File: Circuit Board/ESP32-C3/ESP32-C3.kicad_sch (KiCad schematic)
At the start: 44 parts

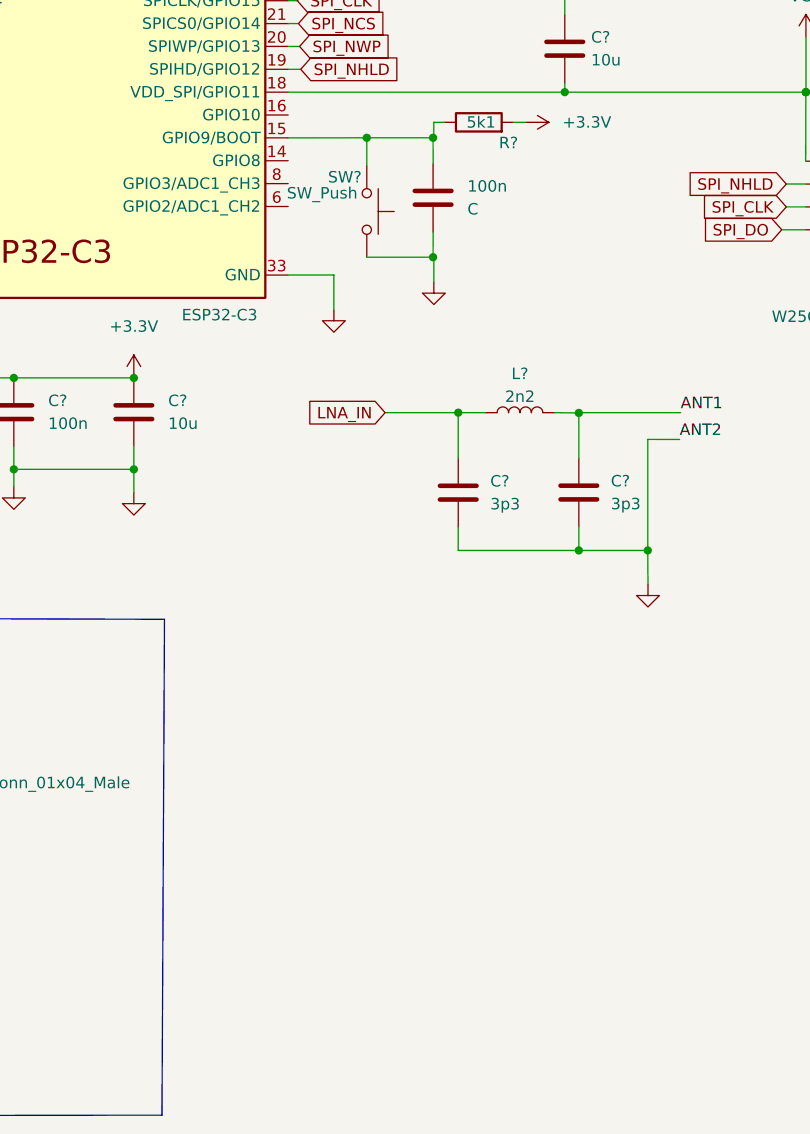
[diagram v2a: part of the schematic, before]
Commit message: Added LED circuits
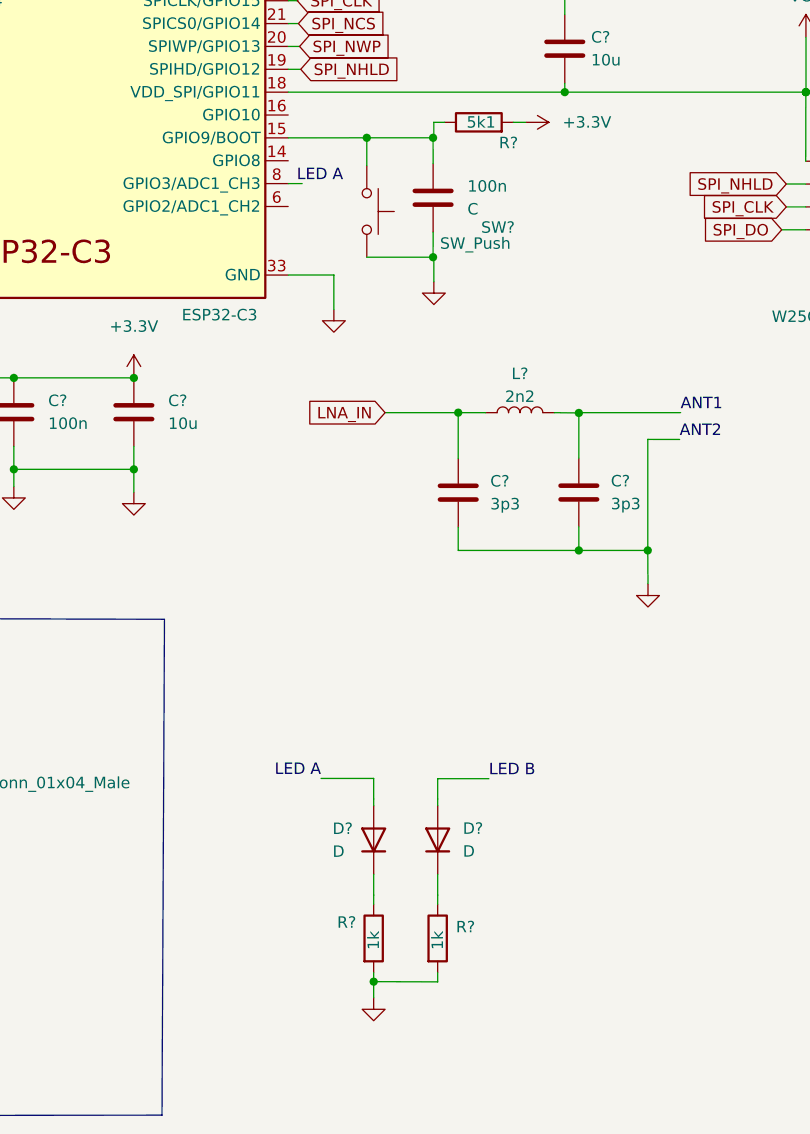
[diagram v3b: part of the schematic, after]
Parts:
- added D? (x2): D, symbol Device:D
- added R? (x2): 1k, symbol Device:R
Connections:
- net +3.3V: now also R?.2, R?.2
- net LED B: now also D?.2 (A)
- net LED A: now reaches U?.8 (GPIO3/ADC1_CH3)
- net LED A: now also D?.2 (A)
- new net: D?.1 (K), R?.1 (x2)

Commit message: Added comments
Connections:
- net at U?.4 (I/O2): now also J?.A6 (D+), J?.B6 (D+)
- no-connect marks 5 -> 8
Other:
- note added: "External 4MB Flash"
- company: (none) -> Sebastian Rincon
- title: (none) -> ESP32-C3
- moved on the sheet: C?, D?, L?, R?

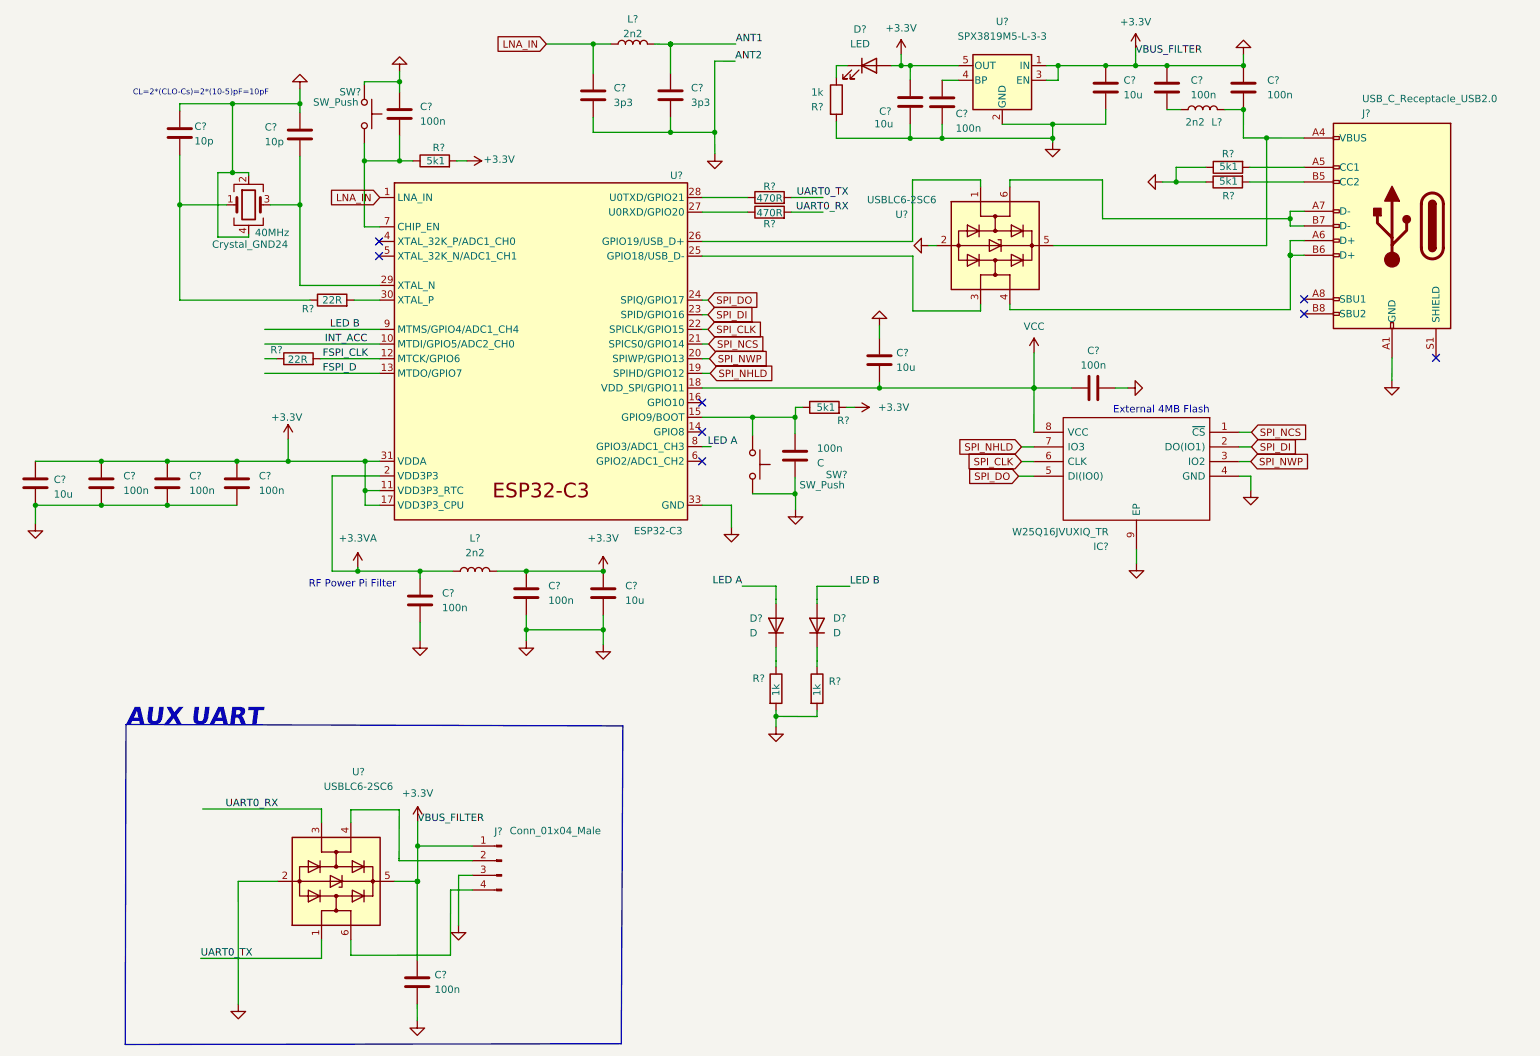
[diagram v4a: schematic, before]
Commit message: Annotated designators
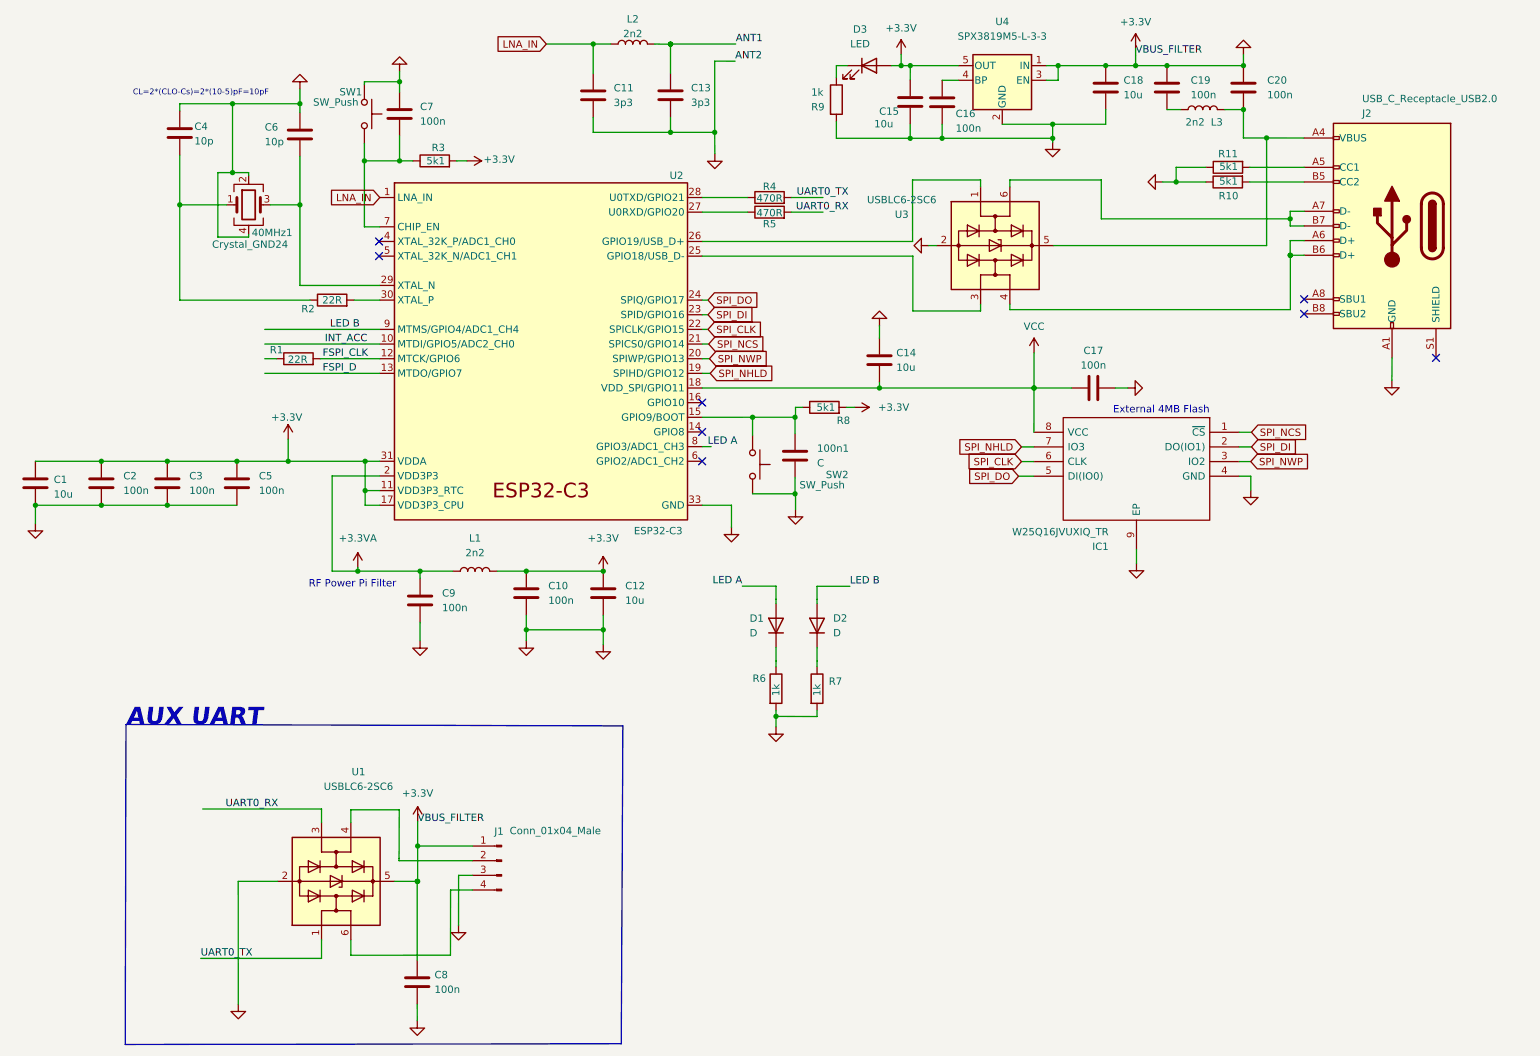
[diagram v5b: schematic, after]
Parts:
- gave numbers to parts that had none: 46
- renumbered 100n to 100n1, 40MHz to 40MHz1

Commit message: Correct ERC errors
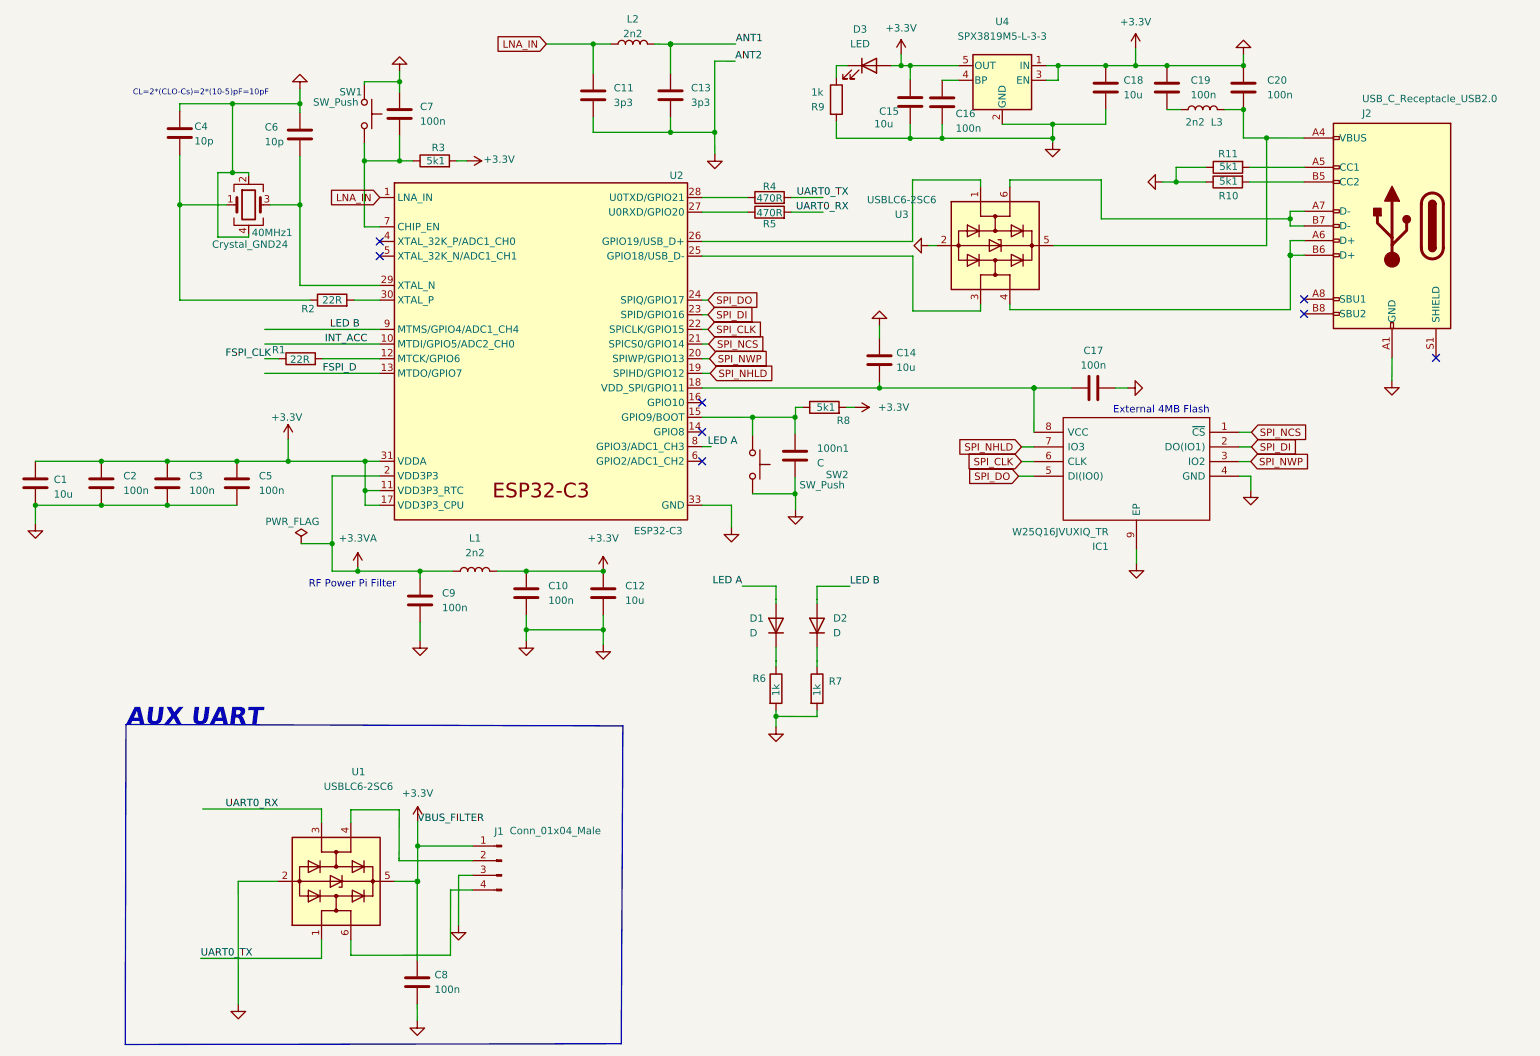
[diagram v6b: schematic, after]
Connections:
- net FSPI_CLK: now also R1.1; no longer R1.2, U2.12 (MTCK/GPIO6)
- net VCC: no longer names the net of C14.2, C17.1, IC1.8 (VCC), U2.18 (VDD_SPI/GPIO11)
- new net: R1.2, U2.12 (MTCK/GPIO6)
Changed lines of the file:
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@@
   (junction (at 32.1564 99.0092) (diameter 0) (color 0 0 0 0)
   )
+  (junction (at 72.1614 105.664) (diameter 0) (color 0 0 0 0)
+  )
   (junction (at 234.1372 35.3411) (diameter 0) (color 0 0 0 0)
   )
@@
   (junction (at 105.8164 110.4392) (diameter 0) (color 0 0 0 0)
   )
+  (no_connect (at 80.4164 55.8292))
+  (no_connect (at 80.4164 53.2892))
   (no_connect (at 240.6396 63.2968))
   (no_connect (at 240.6396 65.8368))
@@
   (no_connect (at 136.2964 86.3092))
   (no_connect (at 136.2964 91.3892))
-  (no_connect (at 80.2894 55.8292))
-  (no_connect (at 80.2894 53.2892))
   (wire (pts (xy 226.8728 30.4292) (xy 230.124 30.4292))
     (stroke (width 0) (type default) (color 0 0 0 0))
@@
     (stroke (width 0) (type default) (color 0 0 0 0))
   )
+  (wire (pts (xy 70.5104 73.6092) (xy 80.4164 73.6092))
+    (stroke (width 0) (type default) (color 0 0 0 0))
+  )
   (wire (pts (xy 152.4789 82.042) (xy 153.67 82.042))
     (stroke (width 0) (type default) (color 0 0 0 0))
@@
     (stroke (width 0) (type default) (color 0 0 0 0))
   )
-  (wire (pts (xy 193.8274 72.5932) (xy 193.8274 78.6892))
-    (stroke (width 0) (type default) (color 0 0 0 0))
-  )
   (wire (pts (xy 60.4774 68.5292) (xy 80.4164 68.5292))
     (stroke (width 0) (type default) (color 0 0 0 0))
@@
     (stroke (width 0) (type default) (color 0 0 0 0))
   )
+  (wire (pts (xy 72.1614 105.664) (xy 72.1614 110.4392))
+    (stroke (width 0) (type default) (color 0 0 0 0))
+  )
   (wire (pts (xy 172.3623 35.4076) (xy 177.8846 35.4076))
     (stroke (width 0) (type default) (color 0 0 0 0))
@@
     (stroke (width 0) (type default) (color 0 0 0 0))
   )
-  (wire (pts (xy 72.1614 93.9292) (xy 72.1614 110.4392))
+  (wire (pts (xy 72.1614 93.9292) (xy 72.1614 105.664))
     (stroke (width 0) (type default) (color 0 0 0 0))
   )
@@
     (stroke (width 0) (type default) (color 0 0 0 0))
   )
-  (wire (pts (xy 70.1294 73.6092) (xy 80.4164 73.6092))
-    (stroke (width 0) (type default) (color 0 0 0 0))
-  )
   (wire (pts (xy 184.5564 42.6212) (xy 172.7596 42.6212))
     (stroke (width 0) (type default) (color 0 0 0 0))
@@
     (stroke (width 0) (type default) (color 0 0 0 0))
   )
+  (wire (pts (xy 66.802 105.664) (xy 72.1614 105.664))
+    (stroke (width 0) (type default) (color 0 0 0 0))
+  )
   (wire (pts (xy 72.1614 110.4392) (xy 76.6064 110.4392))
     (stroke (width 0) (type default) (color 0 0 0 0))
@@
     (stroke (width 0) (type default) (color 0 0 0 0))
   )
-  (wire (pts (xy 60.4774 73.6092) (xy 62.5094 73.6092))
+  (wire (pts (xy 60.4774 73.6092) (xy 62.8904 73.6092))
     (stroke (width 0) (type default) (color 0 0 0 0))
   )
@@
     (effects (font (size 1.27 1.27)) (justify right bottom))
   )
-  (label "VBUS_FILTER" (at 211.4294 21.0525 0)
-    (effects (font (size 1.27 1.27)) (justify left bottom))
-  )
   (label "VBUS_FILTER" (at 86.9797 154.2376 0)
     (effects (font (size 1.27 1.27)) (justify left bottom))
@@
     (effects (font (size 1.27 1.27)) (justify left bottom))
   )
-  (label "FSPI_CLK" (at 70.5104 73.6092 0)
-    (effects (font (size 1.27 1.27)) (justify left bottom))
+  (label "FSPI_CLK" (at 61.5444 73.6092 180)
+    (effects (font (size 1.27 1.27)) (justify right bottom))
   )
   (label "INT_ACC" (at 70.8914 71.0692 0)
@@
     )
     (property "Datasheet" "" (id 3) (at 95.5294 39.3192 0)
-      (effects (font (size 1.27 1.27)) hide)
-    )
-    (pin "1")
-  )
-  (symbol (lib_id "power:VCC") (at 193.8274 72.5932 0) (unit 1)
-    (in_bom yes) (on_board yes)
-    (property "Reference" "#PWR023" (id 0) (at 193.8274 76.4032 0)
-      (effects (font (size 1.27 1.27)) hide)
-    )
-    (property "Value" "VCC" (id 1) (at 193.8274 68.0212 0))
-    (property "Footprint" "" (id 2) (at 193.8274 72.5932 0)
-      (effects (font (size 1.27 1.27)) hide)
-    )
-    (property "Datasheet" "" (id 3) (at 193.8274 72.5932 0)
       (effects (font (size 1.27 1.27)) hide)
     )
@@
     (pin "1")
   )
+  (symbol (lib_id "power:PWR_FLAG") (at 66.802 105.664 0) (unit 1)
+    (in_bom yes) (on_board yes)
+    (property "Reference" "#FLG0101" (id 0) (at 66.802 103.759 0)
+      (effects (font (size 1.27 1.27)) hide)
+    )
+    (property "Value" "PWR_FLAG" (id 1) (at 65.278 101.854 0))
+    (property "Footprint" "" (id 2) (at 66.802 105.664 0)
+      (effects (font (size 1.27 1.27)) hide)
+    )
+    (property "Datasheet" "~" (id 3) (at 66.802 105.664 0)
+      (effects (font (size 1.27 1.27)) hide)
+    )
+    (pin "1")
+  )
   (symbol (lib_id "Device:C") (at 87.4014 115.5192 0) (unit 1)
     (in_bom yes) (on_board yes) (fields_autoplaced)
@@
     (pin "1")
   )
-  (symbol (lib_id "Device:R") (at 66.3194 73.6092 90) (unit 1)
-    (in_bom yes) (on_board yes)
-    (property "Reference" "R1" (id 0) (at 62.5094 72.0852 90))
-    (property "Value" "22R" (id 1) (at 66.1924 73.7362 90))
-    (property "Footprint" "" (id 2) (at 66.3194 75.3872 90)
-      (effects (font (size 1.27 1.27)) hide)
-    )
-    (property "Datasheet" "~" (id 3) (at 66.3194 73.6092 0)
+  (symbol (lib_id "Device:R") (at 66.7004 73.6092 90) (unit 1)
+    (in_bom yes) (on_board yes)
+    (property "Reference" "R1" (id 0) (at 62.8904 72.0852 90))
+    (property "Value" "22R" (id 1) (at 66.5734 73.7362 90))
+    (property "Footprint" "" (id 2) (at 66.7004 75.3872 90)
+      (effects (font (size 1.27 1.27)) hide)
+    )
+    (property "Datasheet" "~" (id 3) (at 66.7004 73.6092 0)
       (effects (font (size 1.27 1.27)) hide)
     )
@@
   )
   (symbol_instances
+    (path "/45ad7d8f-cc29-4c37-ba94-f8e0d065f1a6"
+      (reference "#FLG0101") (unit 1) (value "PWR_FLAG") (footprint "")
+    )
     (path "/01cd939f-253a-4c9e-9624-0cd1885d52fb"
       (reference "#PWR01") (unit 1) (value "GND") (footprint "")
@@
       (reference "#PWR022") (unit 1) (value "GND") (footprint "")
     )
-    (path "/10368d7d-1130-4393-9cc1-0226bdd6cda1"
-      (reference "#PWR023") (unit 1) (value "VCC") (footprint "")
-    )
     (path "/21338b29-75b2-4a86-b3cb-05591330877c"
